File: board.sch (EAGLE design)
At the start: 109 parts, among them IC1 LMZ10501SILT, IC2 TPS61088RHLR, Q1 IRFML8244TRPBF, Q2 IRFML8244TRPBF, Q3 IRFML8244TRPBF, Q4 IRFML8244TRPBF, Q5 IRFML8244TRPBF, U1 TB6612FNG, U2 MPU6500, U3 STM32F405RG, X1 JST-XH

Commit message: Changed IMU to bosch BMI088
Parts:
- removed C30: 0.1u, CASE-RCL:C0603
- removed R29, R30, R_MOSI, R_SCL, R_SCLK, R_SDA: 0, CASE-RCL:R0603
- removed U2: MPU6500, Isaks Bibliotek:MPU6500
- added U$8, U$9: IE2-1024, Isaks Bibliotek:IE2-1024
- added U4: BMI088, Isaks Bibliotek:BMI088
- C34: value 10n -> 0.1u
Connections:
- removed net !CS: R30.1
- removed net INT: U2.INT
- removed net MISO: U2.AD0/MISO
- removed net MOSI: R_MOSI.1
- removed net N$30: R_SCL.2, R_SCLK.2, U2.SCL/SCLK
- removed net N$36: R29.2, R30.2, U2.!CS
- removed net SCLK: R_SCLK.1
- new net A0_ACCEL: U4.SDO1
- new net A0_GYRO: U4.SDO2
- new net INT1_ACC: U4.INT1
- new net INT1_GYRO: U4.INT3
- new net INT2_ACCEL: U4.INT2
- new net INT2_GYRO: U4.INT4
- net 3.3VA: now also U4.CSB1, U4.PS, U4.VDD, U4.VDDIO; no longer R29.1, U2.VDD, U2.VDDIO
- net GND_A: now also U4.GNDA, U4.GNDIO; no longer C30.2, U2.FSYNC, U2.GND, U2.RESV
- net N$28: now also U3.NRST, U3.PA0_WKUP, U3.PA1, U3.PA2, U3.PA3, U3.PA4, U3.PA5, U3.PA6, U3.PA7, U3.PB0, U3.PB1, U3.PB10, U3.PB11, U3.PB2, U3.PC0, U3.PC1, U3.PC13-TAMPER-RTC, U3.PC14-OSC32_IN, U3.PC15-OSC32_OUT, U3.PC2, U3.PC3, U3.PC4, U3.PC5, U3.PH0_OSC_IN, U3.PH1_OSC_OUT, U3.VBAT, U3.VDDA, U3.VDD_1, U3.VDD_4, U3.VSSA, U3.VSS_1, U3.VSS_4; no longer C30.1, U2.REGOUT
- net N$29: now also U3.BOOT0, U3.PA10, U3.PA11, U3.PA12, U3.PA13, U3.PA14, U3.PA15, U3.PA8, U3.PA9, U3.PB12, U3.PB13, U3.PB14, U3.PB15, U3.PB3, U3.PB4, U3.PB5, U3.PB6, U3.PB7, U3.PB8, U3.PB9, U3.PC10, U3.PC11, U3.PC12, U3.PC6, U3.PC7, U3.PC8, U3.PC9, U3.PD2, U3.VDD_2, U3.VDD_3, U3.VSS_2, U3.VSS_3; no longer R_MOSI.2, R_SDA.2, U2.SDA/MOSI
- net SCL: now also U4.SCL/SCK; no longer R_SCL.1
- net SDA: now also U4.SDA/SDI; no longer R_SDA.1
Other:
- note added: "I2C mode"
- note added: "IMU Bosch - BMI088"
- note removed: "Gyro MPU6050"
- note removed: "Most MPU6050/6500 libraries use I2C but SPI is faster/better? there is confiburable 0 ohm resistors to choose which interface to use."
- moved on the sheet: C34, C35, U3

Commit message: Pin Setup on MCU
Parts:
- removed U$8, U$9: IE2-1024, Isaks Bibliotek:IE2-1024
- added C30, C37, C38, C39, C40, C42, C43: 0.1u, CASE-RCL:C0603
- added C36, C44: 1u, CASE-RCL:C0603
- added C41: 10u, CASE-RCL:C0603
- added JP1: (no value), CASE-Pinhead:PINHD-2X3
- added JP2: (no value), CASE-Pinhead:PINHD-2X4
- added MOTOR_LEFT, MOTOR_RIGHT: IDC-6PIN, Isaks Bibliotek:IDC-6PIN
- added R29: 100k, CASE-RCL:R0603
- added R30, R32, R33, R34: 10k, CASE-RCL:R0603
- added S2, S3: KMR621NGLFS, CASE-Switches:KMR621NGLFS
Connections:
- removed net A0_ACCEL: U4.SDO1
- removed net A0_GYRO: U4.SDO2
- removed net INT1_ACC: U4.INT1
- removed net INT1_GYRO: U4.INT3
- removed net INT2_ACCEL: U4.INT2
- removed net INT2_GYRO: U4.INT4
- removed net SCL: U4.SCL/SCK
- removed net SDA: U4.SDA/SDI
- removed net VOLM_BATT: R28.1, R31.2
- removed net VOLM_CELL1: R26.1, R27.2
- new net BOOT0: R34.2
- new net BOOT1: R33.1
- new net BUTTON_SEL: C30.1, R30.2, U3.PB2
- new net CS_ACCEL: U3.PB13, U4.CSB1
- new net CS_GYRO: U3.PB12, U4.CSB2
- new net ENC_L_A: MOTOR_RIGHT.6, U3.PA1
- new net ENC_L_B: MOTOR_RIGHT.5, U3.PA0_WKUP
- new net ENC_R_A: MOTOR_LEFT.6, U3.PA5
- new net ENC_R_B: MOTOR_LEFT.5, U3.PB3
- new net INT_ACCEL: U3.PC4, U4.INT1
- new net INT_GYRO: U3.PC5, U4.INT3
- new net MISO: U3.PB14, U4.SDO1, U4.SDO2
- new net MOSI: U3.PB15, U4.SDA/SDI
- new net N$32: JP1.4, R33.2
- new net N$34: JP1.3, R34.1
- new net N$35: R29.2, R30.1, S2.1, S2.2
- new net RESET: C36.1, R32.1, S3.3, S3.4
- new net RX: JP2.5, U3.PA10
- new net SCK: U3.PB10, U4.SCL/SCK
- new net SWCLK: JP2.6, U3.PA14
- new net SWDIO: JP2.8, U3.PA13
- new net TX: JP2.7, U3.PA9
- new net VOLTM_BATT: R28.1, R31.2, U3.PA3
- new net VOLTM_CELL1: R26.1, R27.2, U3.PA4
- net 3.3V: now also C37.1, C38.1, C39.1, C40.1, C41.1, C42.1, C43.1, C44.1, JP1.1, JP1.2, JP2.1, JP2.2, R29.1, R32.2, U3.VSS_1, U3.VSS_4
- net 3.3VA: no longer U4.CSB1, U4.PS
- net 5V: now also MOTOR_LEFT.4, MOTOR_RIGHT.4
- net BUZZER: now also U3.PA11
- net FL_EMITTER: now also U3.PA7
- net FL_RECEIVER: now also U3.PC1
- net FR_EMITTER: now also U3.PB0
- net FR_RECEIVER: now also U3.PC2
- net GND: now also C30.2, C36.2, C37.2, C38.2, C39.2, C40.2, C41.2, C42.2, C43.2, C44.2, JP1.5, JP1.6, JP2.3, JP2.4, MOTOR_LEFT.3, MOTOR_RIGHT.3, S2.3, S2.4, S3.1, S3.2, U3.VDD_1, U3.VDD_4
- net GND_A: now also U4.PS
- net LED_B: now also U3.PA15
- net LED_G: now also U3.PC10
- net LED_R: now also U3.PC11
- net L_EMITTER: now also U3.PA6
- net L_RECEIVER: now also U3.PC0
- net ML_IN1: now also U3.PB5
- net ML_IN2: now also U3.PB4
- net MOTOR_L_1: now also MOTOR_RIGHT.2
- net MOTOR_L_2: now also MOTOR_RIGHT.1
- net MOTOR_R_1: now also MOTOR_LEFT.2
- net MOTOR_R_2: now also MOTOR_LEFT.1
- net MR_IN1: now also U3.PB7
- net MR_IN2: now also U3.PB6
- net N$28: no longer U3.PA0_WKUP, U3.PA1, U3.PA2, U3.PA3, U3.PA4, U3.PA5, U3.PA6, U3.PA7, U3.PB0, U3.PB1, U3.PB10, U3.PB2, U3.PC0, U3.PC1, U3.PC2, U3.PC3, U3.PC4, U3.PC5, U3.VDD_1, U3.VDD_4, U3.VSS_1, U3.VSS_4
- net N$29: no longer U3.PA10, U3.PA11, U3.PA13, U3.PA14, U3.PA15, U3.PA9, U3.PB12, U3.PB13, U3.PB14, U3.PB15, U3.PB3, U3.PB4, U3.PB5, U3.PB6, U3.PB7, U3.PB8, U3.PB9, U3.PC10, U3.PC11
- net PWM_L: now also U3.PB8
- net PWM_R: now also U3.PB9
- net R_EMITTER: now also U3.PB1
- net R_RECEIVER: now also U3.PC3
- net VOLTM_BOOST: now also U3.PA2
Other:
- note added: "BOOT0=0 BOOT1=x - main flash memory (your uploaded code) BOOT0=1 BOOT1=0 - System momory (internal serial USART1 boot loader) BOOT0=1 BOOT1=1 - Embedded SRAM Applies after reboot"
- note added: "BOOTX"
- note added: "Debounced Button Pull Up - Pulse Low"
- note added: "Debug SWD + UART"
- note added: "Motor Connector IDC-6Pin - DIN41651"
- note added: "Package"
- note added: "Reset Button"
- note added: "SPI mode"
- note added: "VBAT"
- note added: "VDD"
- note added: "VDD must have: [x] 1x Tantalum/Ceramc 10uF for package [x] 1x 100nF(0.1uF) for each VDD pin Connect VBAT to VDD and add: [x] 1x 100nF(0.1uF) ceramic VDDA must have: [x] 1x 100nF(0.1uF) ceramic [x] 1x 1uF ceramic/Tantalum"
- note added: "VDDA"
- note added: "VDDA, VSSA bör vara dragna själva då de går direkt till ADC spänningen."
- note removed: "I2C mode"
- moved on the sheet: 5V_PWR, C1, C2, C26, C27, C28, C29, C3, C31, C32, C33, C34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

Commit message: VSS + VDD
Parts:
- removed C37, C38, C39, C40: 0.1u, CASE-RCL:C0603
- removed C41: 10u, CASE-RCL:C0603
- removed R32: 10k, CASE-RCL:R0603
- added C45, C46: 2.2u, CASE-RCL:C0603
- added C47, C48, C49, C50, C51: 0.1u, CASE-RCL:C0603
- C36: value 1u -> 0.1u
- C42: value 0.1u -> 10u
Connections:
- removed net BUTTON_SEL: C30.1, R30.2, U3.PB2
- new net BTN_SEL: C30.1, R30.2, U3.PD2
- new net N$30: C36.2, S3.1, S3.2
- new net N$36: C45.1, U3.VCAP_1
- new net N$37: C46.1, U3.VCAP_2
- net 3.3V: now also C47.1, C48.1, C49.1, C50.1, C51.1, U3.VBAT, U3.VDD_1, U3.VDD_2, U3.VDD_3, U3.VDD_4; no longer C37.1, C38.1, C39.1, C40.1, C41.1, C43.1, C44.1, R32.2, U3.VSS_1, U3.VSS_4
- net 3.3VA: now also C43.1, C44.1, U3.VDDA
- net BOOT0: now also U3.BOOT0
- net BOOT1: now also U3.PB2
- net GND: now also C45.2, C46.2, C47.2, C48.2, C49.2, C50.2, C51.2, U3.VSS_3, U3.VSS_4; no longer C36.2, C37.2, C38.2, C39.2, C40.2, C41.2, C43.2, C44.2, S3.1, S3.2, U3.VDD_1, U3.VDD_4
- net GND_A: now also C43.2, C44.2, U3.VSSA
- net N$28: no longer U3.NRST, U3.VBAT, U3.VDDA, U3.VSSA
- net N$29: no longer U3.BOOT0, U3.PD2, U3.VDD_2, U3.VDD_3, U3.VSS_2, U3.VSS_3
- net RESET: now also U3.NRST; no longer R32.1
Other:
- note added: "BOOT MODE"
- note added: "Package Bypass"
- note removed: "BOOTX"
- note removed: "Package"
- note removed: "VBAT"
- note removed: "VDD"
- note removed: "VDDA"
- note removed: "VDDA, VSSA bör vara dragna själva då de går direkt till ADC spänningen."
- moved on the sheet: C36, C42, C43, C44, JP1, R33, R34, S3

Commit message: Oled + Hc05
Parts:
- added R32, R35, R36, R37: 10k, CASE-RCL:R0603
- added U$10: WIRELESS-BLUETOOTH-HC-05, diy-modules:WIRELESS-BLUETOOTH-HC-05
- added U$11: DISPLAY-OLED-128X64-I2C, diy-modules:DISPLAY-OLED-128X64-I2C
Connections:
- new net BT_RX: R32.2, U$10.TX
- new net BT_TX: R36.2, U$10.RX
- new net HEADER_RX: R35.2
- new net HEADER_TX: R37.2
- new net SCL: U$11.SCL
- new net SDA: U$11.SDA
- net 5V: now also U$10.+5V, U$11.VCC
- net GND: now also U$10.GND, U$11.GND
- net RX: now also R32.1, R35.1
- net TX: now also R36.1, R37.1
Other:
- note added: "Bluetooth"
- note added: "Choose where to route UART Bluetooth module or Headers with 0 Ohm resistor"
- note added: "User Interface"
- note removed: "User Interface LED + Buzzer + Display?"
- moved on the sheet: C34, C35, C46, C50, U4

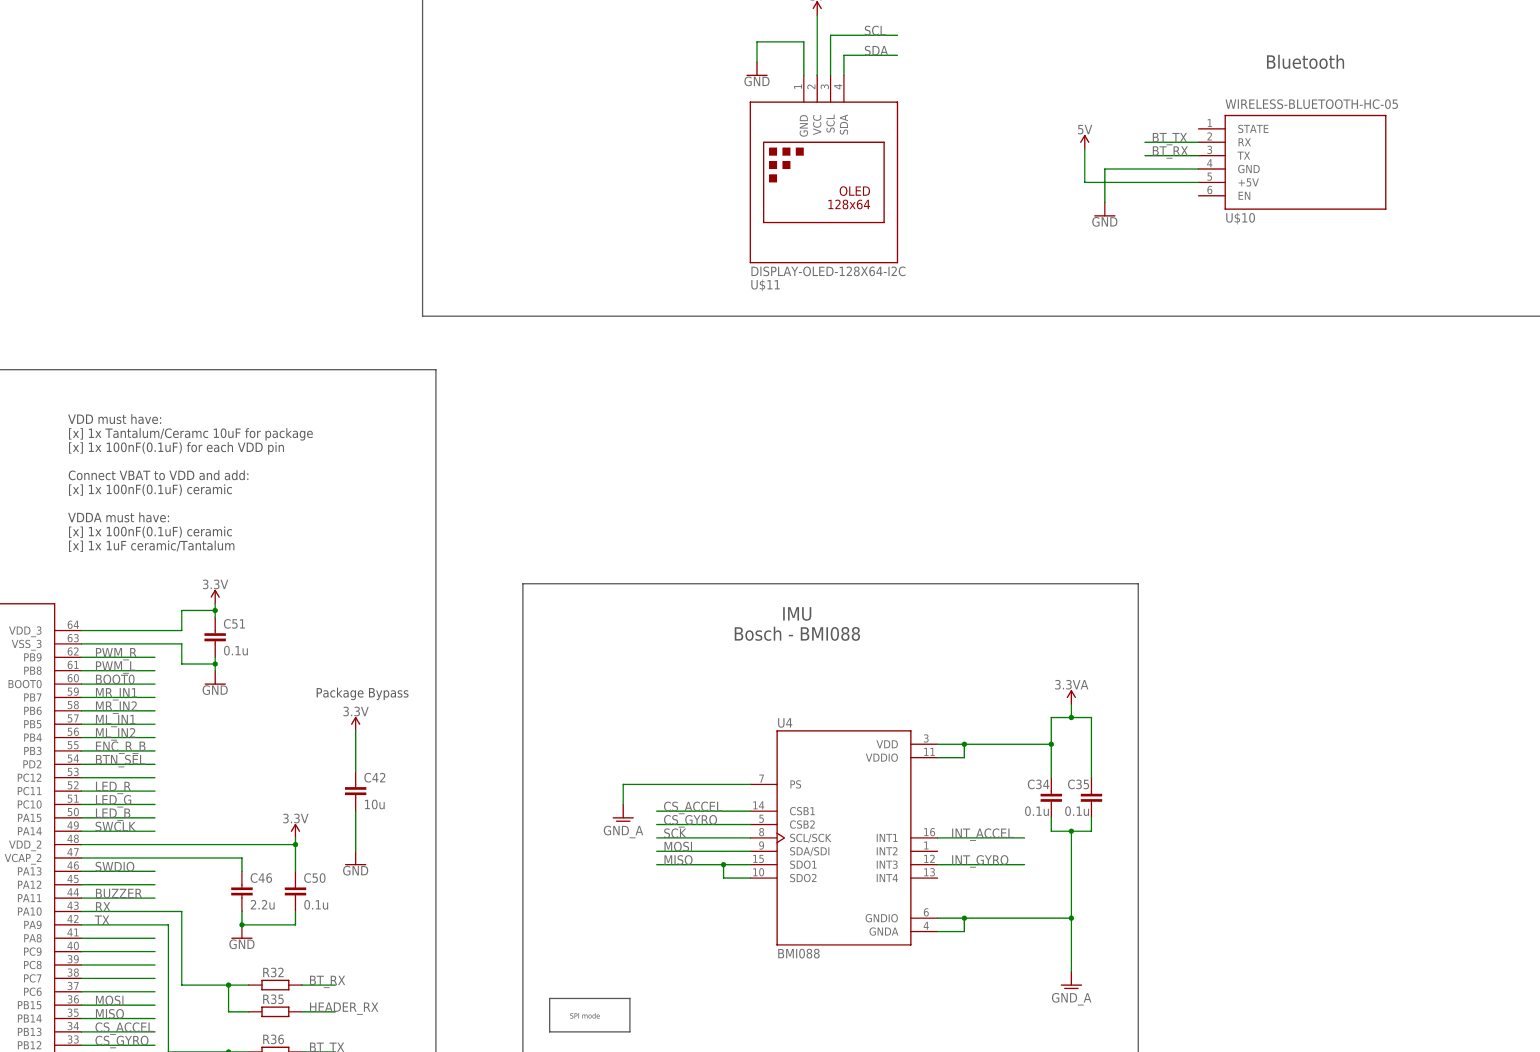
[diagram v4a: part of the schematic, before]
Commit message: Regulator board placement
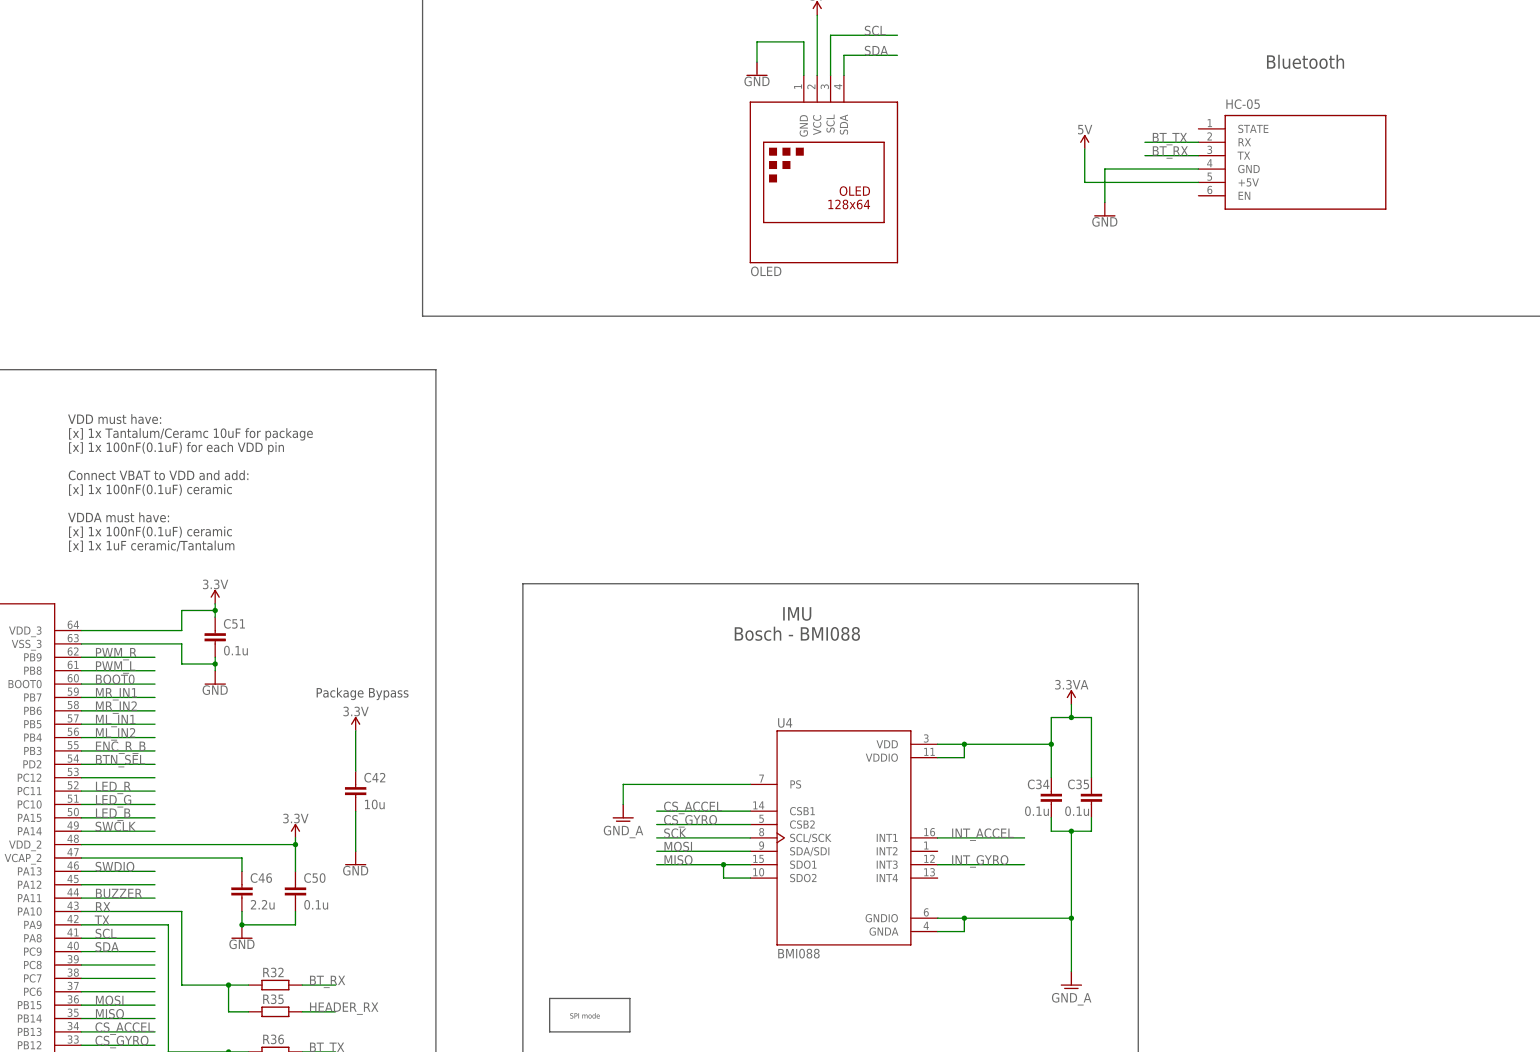
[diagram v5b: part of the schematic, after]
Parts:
- removed U$10: WIRELESS-BLUETOOTH-HC-05, diy-modules:WIRELESS-BLUETOOTH-HC-05
- removed U$11: DISPLAY-OLED-128X64-I2C, diy-modules:DISPLAY-OLED-128X64-I2C
- added HC-05: WIRELESS-BLUETOOTH-HC-05, Isaks Bibliotek:WIRELESS-BLUETOOTH-HC-05
- added OLED: DISPLAY-OLED-128X64-I2C, Isaks Bibliotek:DISPLAY-OLED-128X64-I2C
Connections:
- net 5V: now also HC-05.+5V, OLED.VCC; no longer U$10.+5V, U$11.VCC
- net BT_RX: now also HC-05.TX; no longer U$10.TX
- net BT_TX: now also HC-05.RX; no longer U$10.RX
- net GND: now also HC-05.GND, OLED.GND; no longer U$10.GND, U$11.GND
- net N$29: no longer U3.PA8, U3.PC9
- net SCL: now also OLED.SCL, U3.PA8; no longer U$11.SCL
- net SDA: now also OLED.SDA, U3.PC9; no longer U$11.SDA
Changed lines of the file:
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@@
 <part name="SUPPLY31" library="Isaks Bibliotek" library_urn="urn:adsk.eagle:library:11889733" deviceset="3.3V" device=""/>
 <part name="C51" library="CASE-RCL" deviceset="C0603" device="" package3d_urn="urn:adsk.eagle:package:5332305/1" value="0.1u"/>
-<part name="U$10" library="diy-modules" deviceset="WIRELESS-BLUETOOTH-HC-05" device=""/>
-<part name="U$11" library="diy-modules" deviceset="DISPLAY-OLED-128X64-I2C" device=""/>
 <part name="SUPPLY22" library="Isaks Bibliotek" library_urn="urn:adsk.eagle:library:11889733" deviceset="5V" device=""/>
 <part name="GND32" library="Isaks Bibliotek" library_urn="urn:adsk.eagle:library:11889733" deviceset="GND" device=""/>
@@
 <part name="R36" library="CASE-RCL" deviceset="R0603" device="" package3d_urn="urn:adsk.eagle:package:5332309/1" value="10k"/>
 <part name="R37" library="CASE-RCL" deviceset="R0603" device="" package3d_urn="urn:adsk.eagle:package:5332309/1" value="10k"/>
+<part name="OLED" library="Isaks Bibliotek" library_urn="urn:adsk.eagle:library:11889733" deviceset="DISPLAY-OLED-128X64-I2C" device=""/>
+<part name="HC-05" library="Isaks Bibliotek" library_urn="urn:adsk.eagle:library:11889733" deviceset="WIRELESS-BLUETOOTH-HC-05" device=""/>
 </parts>
 <sheets>
@@
 <attribute name="VALUE" x="35.814" y="-125.349" size="1.778" layer="96"/>
 </instance>
-<instance part="U$10" gate="G$1" x="241.3" y="-30.48" smashed="yes">
-<attribute name="NAME" x="226.06" y="-43.18" size="1.778" layer="95"/>
-<attribute name="VALUE" x="226.06" y="-21.59" size="1.778" layer="96"/>
-</instance>
-<instance part="U$11" gate="G$1" x="151.13" y="-35.56" smashed="yes">
-<attribute name="NAME" x="135.89" y="-55.88" size="1.778" layer="95"/>
-<attribute name="VALUE" x="135.89" y="-53.34" size="1.778" layer="96"/>
-</instance>
 <instance part="SUPPLY22" gate="G$1" x="199.39" y="-29.21" smashed="yes">
 <attribute name="VALUE" x="199.39" y="-26.416" size="1.778" layer="96" align="bottom-center"/>
@@
 <instance part="R37" gate="G$1" x="45.72" y="-205.74" smashed="yes">
 <attribute name="NAME" x="43.18" y="-204.2414" size="1.778" layer="95"/>
+</instance>
+<instance part="OLED" gate="G$1" x="151.13" y="-35.56" smashed="yes">
+<attribute name="NAME" x="135.89" y="-53.34" size="1.778" layer="95"/>
+</instance>
+<instance part="HC-05" gate="G$1" x="241.3" y="-30.48" smashed="yes">
+<attribute name="NAME" x="226.06" y="-21.59" size="1.778" layer="95"/>
 </instance>
 </instances>
@@
 </segment>
 <segment>
-<pinref part="U$10" gate="G$1" pin="GND"/>
 <wire x1="220.98" y1="-33.02" x2="203.2" y2="-33.02" width="0.1524" layer="91"/>
 <pinref part="GND32" gate="1" pin="GND"/>
 <wire x1="203.2" y1="-33.02" x2="203.2" y2="-39.37" width="0.1524" layer="91"/>
-</segment>
-<segment>
-<pinref part="U$11" gate="G$1" pin="GND"/>
+<pinref part="HC-05" gate="G$1" pin="GND"/>
+</segment>
+<segment>
 <wire x1="146.05" y1="-15.24" x2="146.05" y2="-8.89" width="0.1524" layer="91"/>
 <wire x1="146.05" y1="-8.89" x2="137.16" y2="-8.89" width="0.1524" layer="91"/>
 <wire x1="137.16" y1="-8.89" x2="137.16" y2="-12.7" width="0.1524" layer="91"/>
 <pinref part="GND33" gate="1" pin="GND"/>
+<pinref part="OLED" gate="G$1" pin="GND"/>
 </segment>
 </net>
@@
 </segment>
 <segment>
-<pinref part="U$10" gate="G$1" pin="+5V"/>
 <wire x1="220.98" y1="-35.56" x2="199.39" y2="-35.56" width="0.1524" layer="91"/>
 <pinref part="SUPPLY22" gate="G$1" pin="5V"/>
 <wire x1="199.39" y1="-35.56" x2="199.39" y2="-29.21" width="0.1524" layer="91"/>
-</segment>
-<segment>
-<pinref part="U$11" gate="G$1" pin="VCC"/>
+<pinref part="HC-05" gate="G$1" pin="+5V"/>
+</segment>
+<segment>
 <wire x1="148.59" y1="-15.24" x2="148.59" y2="-3.81" width="0.1524" layer="91"/>
 <pinref part="SUPPLY25" gate="G$1" pin="5V"/>
+<pinref part="OLED" gate="G$1" pin="VCC"/>
 </segment>
 </net>
@@
 </segment>
 <segment>
-<wire x1="22.86" y1="-179.07" x2="8.89" y2="-179.07" width="0.1524" layer="91"/>
-<pinref part="U3" gate="STM32F405RG" pin="PA8"/>
-</segment>
-<segment>
-<wire x1="22.86" y1="-181.61" x2="8.89" y2="-181.61" width="0.1524" layer="91"/>
-<pinref part="U3" gate="STM32F405RG" pin="PC9"/>
-</segment>
-<segment>
 <wire x1="22.86" y1="-184.15" x2="8.89" y2="-184.15" width="0.1524" layer="91"/>
 <pinref part="U3" gate="STM32F405RG" pin="PC8"/>
@@
 <net name="SCL" class="0">
 <segment>
-<pinref part="U$11" gate="G$1" pin="SCL"/>
 <wire x1="151.13" y1="-15.24" x2="151.13" y2="-7.62" width="0.1524" layer="91"/>
 <wire x1="151.13" y1="-7.62" x2="163.83" y2="-7.62" width="0.1524" layer="91"/>
 <label x="157.48" y="-7.62" size="1.778" layer="95"/>
+<pinref part="OLED" gate="G$1" pin="SCL"/>
+</segment>
+<segment>
+<wire x1="22.86" y1="-179.07" x2="8.89" y2="-179.07" width="0.1524" layer="91"/>
+<pinref part="U3" gate="STM32F405RG" pin="PA8"/>
+<label x="11.43" y="-179.07" size="1.778" layer="95"/>
 </segment>
 </net>
 <net name="SDA" class="0">
 <segment>
-<pinref part="U$11" gate="G$1" pin="SDA"/>
 <wire x1="153.67" y1="-15.24" x2="153.67" y2="-11.43" width="0.1524" layer="91"/>
 <wire x1="153.67" y1="-11.43" x2="163.83" y2="-11.43" width="0.1524" layer="91"/>
 <label x="157.48" y="-11.43" size="1.778" layer="95"/>
+<pinref part="OLED" gate="G$1" pin="SDA"/>
+</segment>
+<segment>
+<wire x1="22.86" y1="-181.61" x2="8.89" y2="-181.61" width="0.1524" layer="91"/>
+<pinref part="U3" gate="STM32F405RG" pin="PC9"/>
+<label x="11.43" y="-181.61" size="1.778" layer="95"/>
 </segment>
 </net>
@@
 </segment>
 <segment>
-<pinref part="U$10" gate="G$1" pin="TX"/>
 <wire x1="220.98" y1="-30.48" x2="210.82" y2="-30.48" width="0.1524" layer="91"/>
 <label x="212.09" y="-30.48" size="1.778" layer="95"/>
+<pinref part="HC-05" gate="G$1" pin="TX"/>
 </segment>
 </net>
@@
 </segment>
 <segment>
-<pinref part="U$10" gate="G$1" pin="RX"/>
 <wire x1="220.98" y1="-27.94" x2="210.82" y2="-27.94" width="0.1524" layer="91"/>
 <label x="212.09" y="-27.94" size="1.778" layer="95"/>
-</segment>
-</net>
+<pinref part="HC-05" gate="G$1" pin="RX"/>
+</segment>
+</net>

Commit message: switch layout on board
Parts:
- R32, R35, R36, R37: value 10k -> 0
- renumbered JP2 to DEBUG, S2 to BTN_SEL, S3 to BTN_RST
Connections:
- removed net N$26: C33.2, R25.1, R_FBB.1
- net GND: now also C33.2, R25.1, R_FBB.1
- net N$38: now also SW.1; no longer SW.3
- net V_BAT: now also SW.3; no longer SW.1
